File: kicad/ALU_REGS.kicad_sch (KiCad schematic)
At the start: 40 parts, among them U38 SN74LVC2G157DCU3, U39 SN74LVC2G157DCU3, U40 SN74LVC2G157DCU3, U41 SN74LVC2G157DCU3, U42 SN74LVC2G157DCU3, U43 SN74LVC2G157DCU3, U44 SN74LVC2G157DCU3, U45 SN74LVC2G157DCU3, U46 SN74LVC2G157DCU3, U47 SN74LVC2G157DCU3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

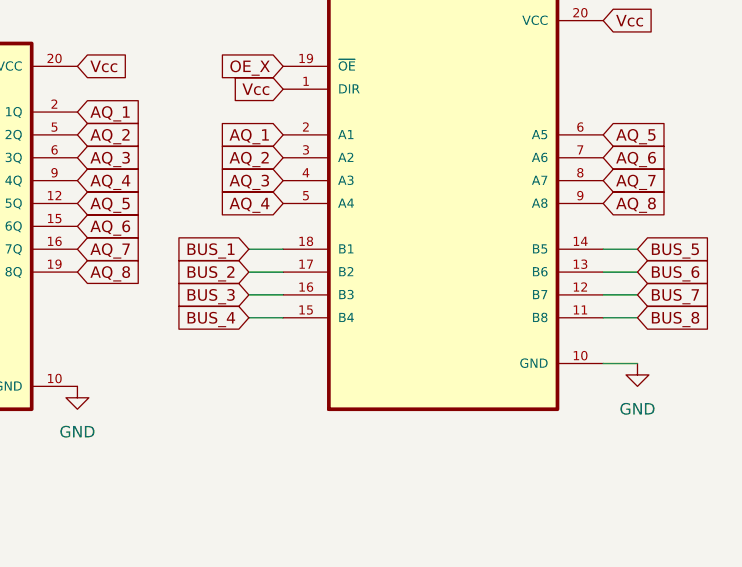
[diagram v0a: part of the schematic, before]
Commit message: update schematic
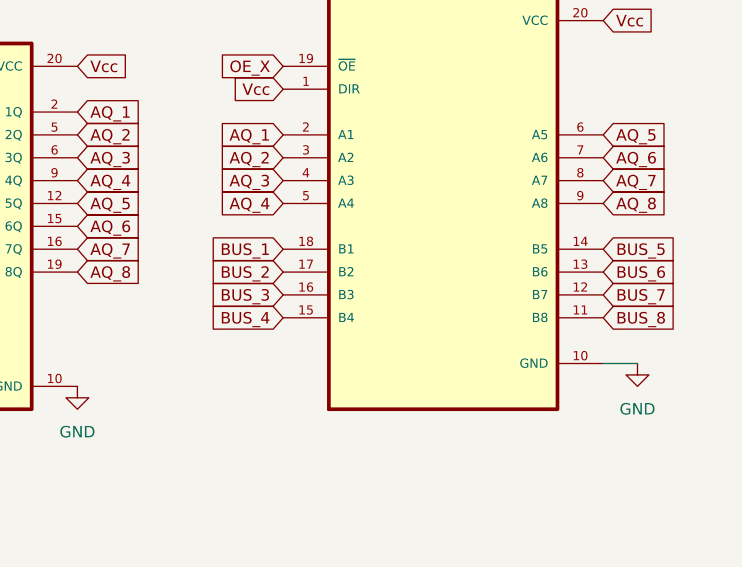
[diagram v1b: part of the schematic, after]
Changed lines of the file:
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@@
 	(wire
 		(pts
-			(xy 223.52 58.42) (xy 227.33 58.42)
-		)
-		(stroke
-			(width 0)
-			(type default)
-		)
-	)
-	(wire
-		(pts
 			(xy 83.82 38.1) (xy 77.47 38.1)
 		)
@@
 	(wire
 		(pts
-			(xy 262.89 58.42) (xy 266.7 58.42)
-		)
-		(stroke
-			(width 0)
-			(type default)
-		)
-	)
-	(wire
-		(pts
 			(xy 189.23 135.89) (xy 189.23 129.54)
 		)
@@
 	(wire
 		(pts
-			(xy 223.52 60.96) (xy 227.33 60.96)
-		)
-		(stroke
-			(width 0)
-			(type default)
-		)
-	)
-	(wire
-		(pts
-			(xy 262.89 55.88) (xy 266.7 55.88)
-		)
-		(stroke
-			(width 0)
-			(type default)
-		)
-	)
-	(wire
-		(pts
-			(xy 223.52 55.88) (xy 227.33 55.88)
-		)
-		(stroke
-			(width 0)
-			(type default)
-		)
-	)
-	(wire
-		(pts
-			(xy 223.52 63.5) (xy 227.33 63.5)
-		)
-		(stroke
-			(width 0)
-			(type default)
-		)
-	)
-	(wire
-		(pts
 			(xy 189.23 129.54) (xy 200.66 129.54)
 		)
@@
 	(wire
 		(pts
-			(xy 262.89 63.5) (xy 266.7 63.5)
-		)
-		(stroke
-			(width 0)
-			(type default)
-		)
-	)
-	(wire
-		(pts
 			(xy 189.23 153.67) (xy 191.77 153.67)
 		)
@@
 	(wire
 		(pts
-			(xy 262.89 60.96) (xy 266.7 60.96)
-		)
-		(stroke
-			(width 0)
-			(type default)
-		)
-	)
-	(wire
-		(pts
 			(xy 193.04 137.16) (xy 200.66 137.16)
 		)
@@
 	(global_label "BUS_8"
 		(shape input)
-		(at 266.7 63.5 0)
+		(at 262.89 63.5 0)
 		(fields_autoplaced yes)
 		(effects
@@
 		)
 		(property "Intersheetrefs" "${INTERSHEET_REFS}"
-			(at 275.6723 63.5 0)
+			(at 271.8623 63.5 0)
 			(effects
 				(font
@@
 	(global_label "BUS_4"
 		(shape input)
-		(at 223.52 63.5 180)
+		(at 227.33 63.5 180)
 		(fields_autoplaced yes)
 		(effects
@@
 		)
 		(property "Intersheetrefs" "${INTERSHEET_REFS}"
-			(at 214.5477 63.5 0)
+			(at 218.3577 63.5 0)
 			(effects
 				(font
@@
 	(global_label "BUS_2"
 		(shape input)
-		(at 223.52 58.42 180)
+		(at 227.33 58.42 180)
 		(fields_autoplaced yes)
 		(effects
@@
 		)
 		(property "Intersheetrefs" "${INTERSHEET_REFS}"
-			(at 214.5477 58.42 0)
+			(at 218.3577 58.42 0)
 			(effects
 				(font
@@
 	(global_label "BUS_7"
 		(shape input)
-		(at 266.7 60.96 0)
+		(at 262.89 60.96 0)
 		(fields_autoplaced yes)
 		(effects
@@
 		)
 		(property "Intersheetrefs" "${INTERSHEET_REFS}"
-			(at 275.6723 60.96 0)
+			(at 271.8623 60.96 0)
 			(effects
 				(font
@@
 	(global_label "BUS_5"
 		(shape input)
-		(at 266.7 55.88 0)
+		(at 262.89 55.88 0)
 		(fields_autoplaced yes)
 		(effects
@@
 		)
 		(property "Intersheetrefs" "${INTERSHEET_REFS}"
-			(at 275.6723 55.88 0)
+			(at 271.8623 55.88 0)
 			(effects
 				(font
@@
 	(global_label "BUS_1"
 		(shape input)
-		(at 223.52 55.88 180)
+		(at 227.33 55.88 180)
 		(fields_autoplaced yes)
 		(effects
@@
 		)
 		(property "Intersheetrefs" "${INTERSHEET_REFS}"
-			(at 214.5477 55.88 0)
+			(at 218.3577 55.88 0)
 			(effects
 				(font
@@
 	(global_label "BUS_3"
 		(shape input)
-		(at 223.52 60.96 180)
+		(at 227.33 60.96 180)
 		(fields_autoplaced yes)
 		(effects
@@
 		)
 		(property "Intersheetrefs" "${INTERSHEET_REFS}"
-			(at 214.5477 60.96 0)
+			(at 218.3577 60.96 0)
 			(effects
 				(font
@@
 	(global_label "BUS_6"
 		(shape input)
-		(at 266.7 58.42 0)
+		(at 262.89 58.42 0)
 		(fields_autoplaced yes)
 		(effects
@@
 		)
 		(property "Intersheetrefs" "${INTERSHEET_REFS}"
-			(at 275.6723 58.42 0)
+			(at 271.8623 58.42 0)
 			(effects
 				(font
